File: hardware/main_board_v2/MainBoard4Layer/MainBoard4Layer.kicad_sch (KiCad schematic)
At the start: 67 parts, among them J1 5V In, J11 Conn_01x01, J12 GREEN, J13 Conn_01x05, J14 Conn_01x04, J2 9V In, J7 Conn_01x02, J8 Conn_01x10, J9 Conn_01x02, U1 TPIC6595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

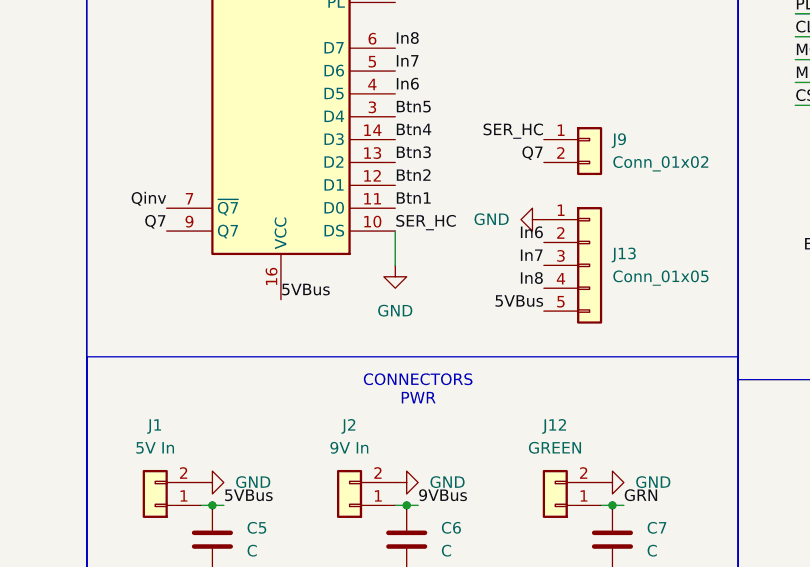
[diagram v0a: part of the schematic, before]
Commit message: Created a version 2 for the bps board to incorporate the improvements, added the symobls and footprint
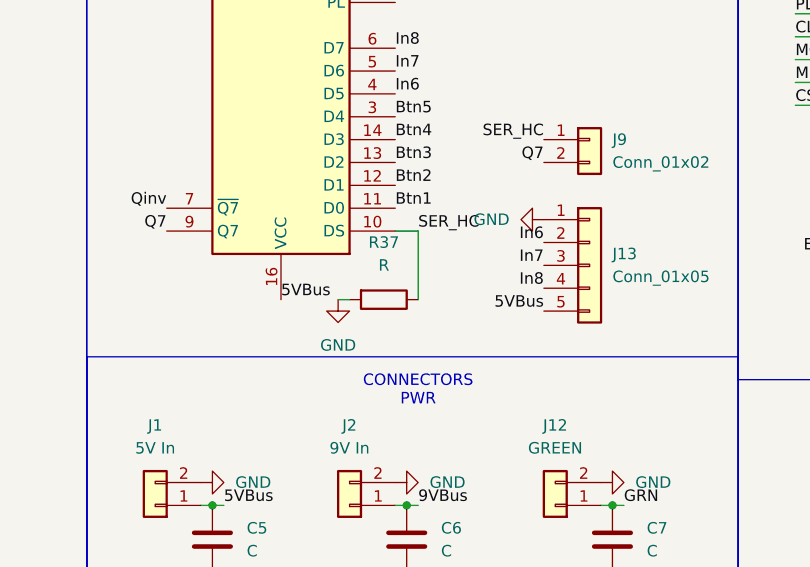
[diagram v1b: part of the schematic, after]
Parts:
- added R37: R, Resistor_SMD:R_1206_3216Metric_Pad1.30x1.75mm_HandSolder, symbol Device:R
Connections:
- net GND: now also R37.2; no longer J9.1 (Pin_1), U7.10 (DS)
- new net SER_HC: J9.1 (Pin_1), R37.1, U7.10 (DS)
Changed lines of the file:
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@@
 	(wire
 		(pts
+			(xy 139.7 147.32) (xy 137.16 147.32)
+		)
+		(stroke
+			(width 0)
+			(type default)
+		)
+	)
+	(wire
+		(pts
 			(xy 218.44 33.02) (xy 222.25 33.02)
 		)
@@
 	(wire
 		(pts
-			(xy 27.94 134.62) (xy 24.13 134.62)
+			(xy 130.81 154.94) (xy 132.08 154.94)
 		)
 		(stroke
@@
 	(wire
 		(pts
-			(xy 137.16 147.32) (xy 137.16 151.13)
+			(xy 27.94 134.62) (xy 24.13 134.62)
 		)
 		(stroke
@@
 	(wire
 		(pts
+			(xy 139.7 147.32) (xy 139.7 154.94)
+		)
+		(stroke
+			(width 0)
+			(type default)
+		)
+	)
+	(wire
+		(pts
 			(xy 184.15 113.03) (xy 184.15 115.57)
 		)
@@
 	)
 	(label "SER_HC"
-		(at 137.16 147.32 0)
+		(at 139.7 147.32 0)
 		(effects
 			(font
@@
 	)
 	(symbol
+		(lib_id "Device:R")
+		(at 135.89 154.94 270)
+		(unit 1)
+		(exclude_from_sim no)
+		(in_bom yes)
+		(on_board yes)
+		(dnp no)
+		(fields_autoplaced yes)
+		(property "Reference" "R37"
+			(at 135.89 148.59 90)
+			(effects
+				(font
+					(size 1.27 1.27)
+				)
+			)
+		)
+		(property "Value" "R"
+			(at 135.89 151.13 90)
+			(effects
+				(font
+					(size 1.27 1.27)
+				)
+			)
+		)
+		(property "Footprint" "Resistor_SMD:R_1206_3216Metric_Pad1.30x1.75mm_HandSolder"
+			(at 135.89 153.162 90)
+			(effects
+				(font
+					(size 1.27 1.27)
+				)
+				(hide yes)
+			)
+		)
+		(property "Datasheet" "~"
+			(at 135.89 154.94 0)
+			(effects
+				(font
+					(size 1.27 1.27)
+				)
+				(hide yes)
+			)
+		)
+		(property "Description" "Resistor"
+			(at 135.89 154.94 0)
+			(effects
+				(font
+					(size 1.27 1.27)
+				)
+				(hide yes)
+			)
+		)
+		(pin "1"
+		)
+		(pin "2"
+		)
+		(instances
+			(project ""
+				(path "/a68a42c8-0d52-4a7d-8bde-897121bcc70e"
+					(reference "R37")
+					(unit 1)
+				)
+			)
+		)
+	)
+	(symbol
 		(lib_id "GregSyms:SD_Breakout")
 		(at 227.33 134.62 0)
@@
 	(symbol
 		(lib_id "power:GND")
-		(at 137.16 151.13 0)
+		(at 130.81 154.94 0)
 		(unit 1)
 		(exclude_from_sim no)
@@
 		(fields_autoplaced yes)
 		(property "Reference" "#PWR028"
-			(at 137.16 157.48 0)
+			(at 130.81 161.29 0)
 			(effects
 				(font
@@
 		)
 		(property "Value" "GND"
-			(at 137.16 156.21 0)
+			(at 130.81 160.02 0)
 			(effects
 				(font
@@
 		)
 		(property "Footprint" ""
-			(at 137.16 151.13 0)
+			(at 130.81 154.94 0)
 			(effects
 				(font
@@
 		)
 		(property "Datasheet" ""
-			(at 137.16 151.13 0)
+			(at 130.81 154.94 0)
 			(effects
 				(font
@@
 		)
 		(property "Description" "Power symbol creates a global label with name \"GND\" , ground"
-			(at 137.16 151.13 0)
+			(at 130.81 154.94 0)
 			(effects
 				(font
@@
 		)
 		(instances
-			(project ""
+			(project "MainBoard4Layer"
 				(path "/a68a42c8-0d52-4a7d-8bde-897121bcc70e"
 					(reference "#PWR028")
